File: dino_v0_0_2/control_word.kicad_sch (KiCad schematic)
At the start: 3 parts, among them U28 74LS138, U29 74LS138, U30 74LS138

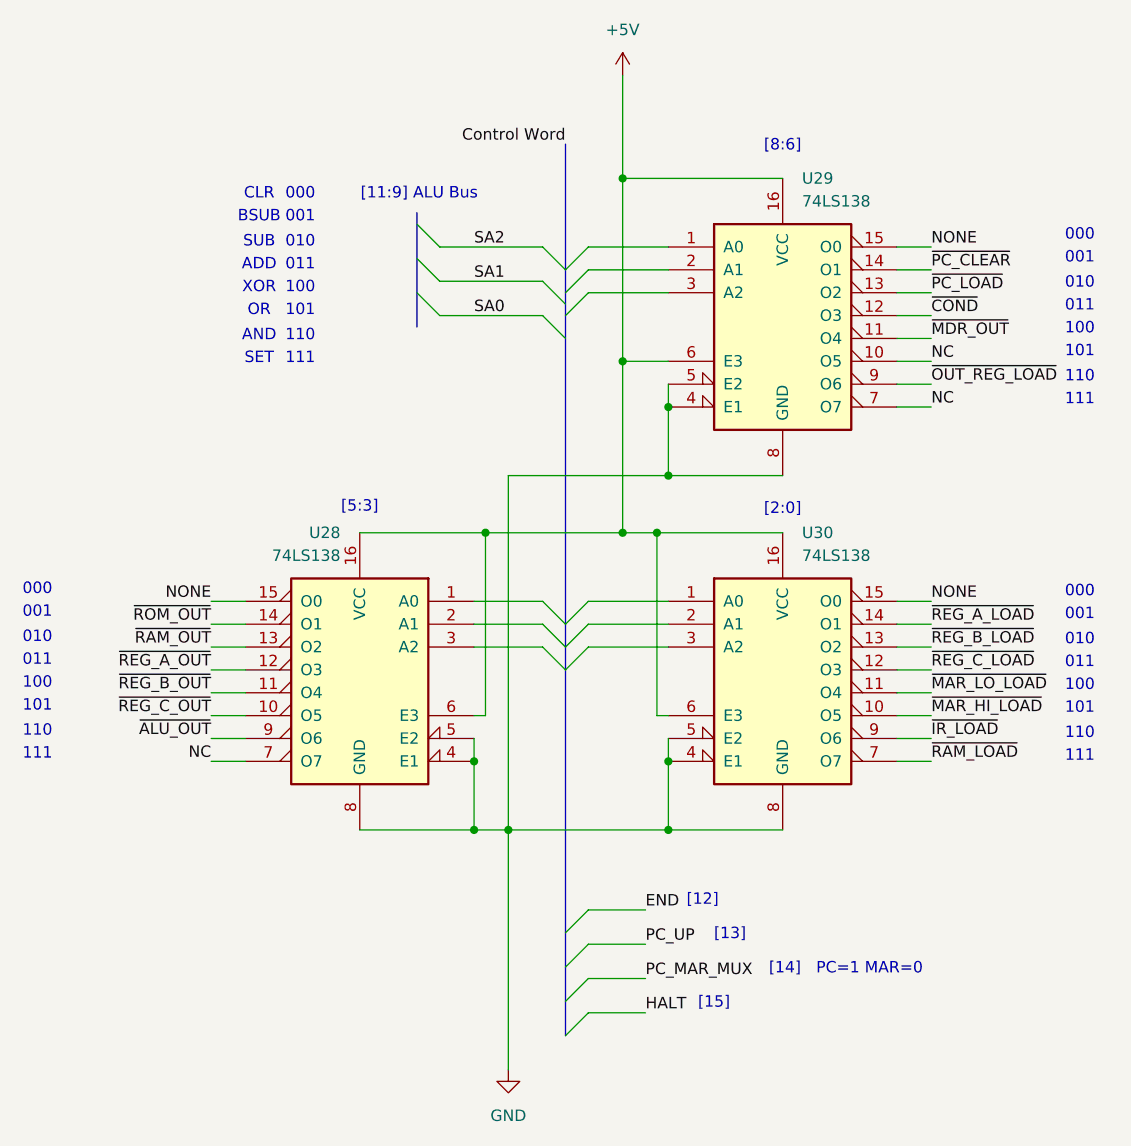
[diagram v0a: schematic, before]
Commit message: DINO v0.0.3: complete ALU/control-word, add MAR+reset sheets, wire reset circuit
ALU sheet: flags register moved from '173 (not in stock) to '273 + a '157
mux to emulate the missing load-enable pins; Z-detect built from a NOR+AND
De Morgan tree instead of a '260; ALU_CIN built from NAND(SA1,SA0) reusing
two already-placed spare gates instead of a dedicated XOR/'86. Sheet is
now fully wired and netlist-clean.

Control word sheet: all 16 CW bits assigned and wired (3x '138 decoders
for the load/source/misc fields, direct bus taps for HALT/PC_MAR_MUX/
PC_UP/END and the ALU SA[2:0] select). Found and fixed several cross-
sheet signal-name mismatches this uncovered (OUT_REG_LOAD/REG_OUT_LOAD,
PC_MAR_MUX/PC_MUX, T-state counter labels, a mirror-reversed IRB->ROM-
address buffer in microcode).

New: MAR and reset sheets, wired into the root hierarchy. Reset circuit
is a from-scratch design: RC+button+74HC14 Schmitt front end feeds the
async PRESET of the clock cluster's spare '74 half (U27B), synchronizing
release to CLK; its Q/~Q fan out to the flags register, the T-state
counter's clear, and (OR'd with the existing microcode-driven PC_CLEAR,
reusing spare gates on the same '02) the PC counters' clear.

Deprecated 7 schematic files no longer referenced by the root sheet's
hierarchy into dino_v0_0_2/deprecated/. Added docs/notes/kicad_netlist.py,
a .kicad_sch connectivity auditor (pin/net resolution incl. buses and
same-name local-label merging) used throughout this session to find the
above bugs; archived completed-work docs into docs/notes/Done/ and
rewrote dino_session_state.md as the current authoritative state+TODO.

Co-Authored-By: Claude Sonnet 5 <noreply@anthropic.com>
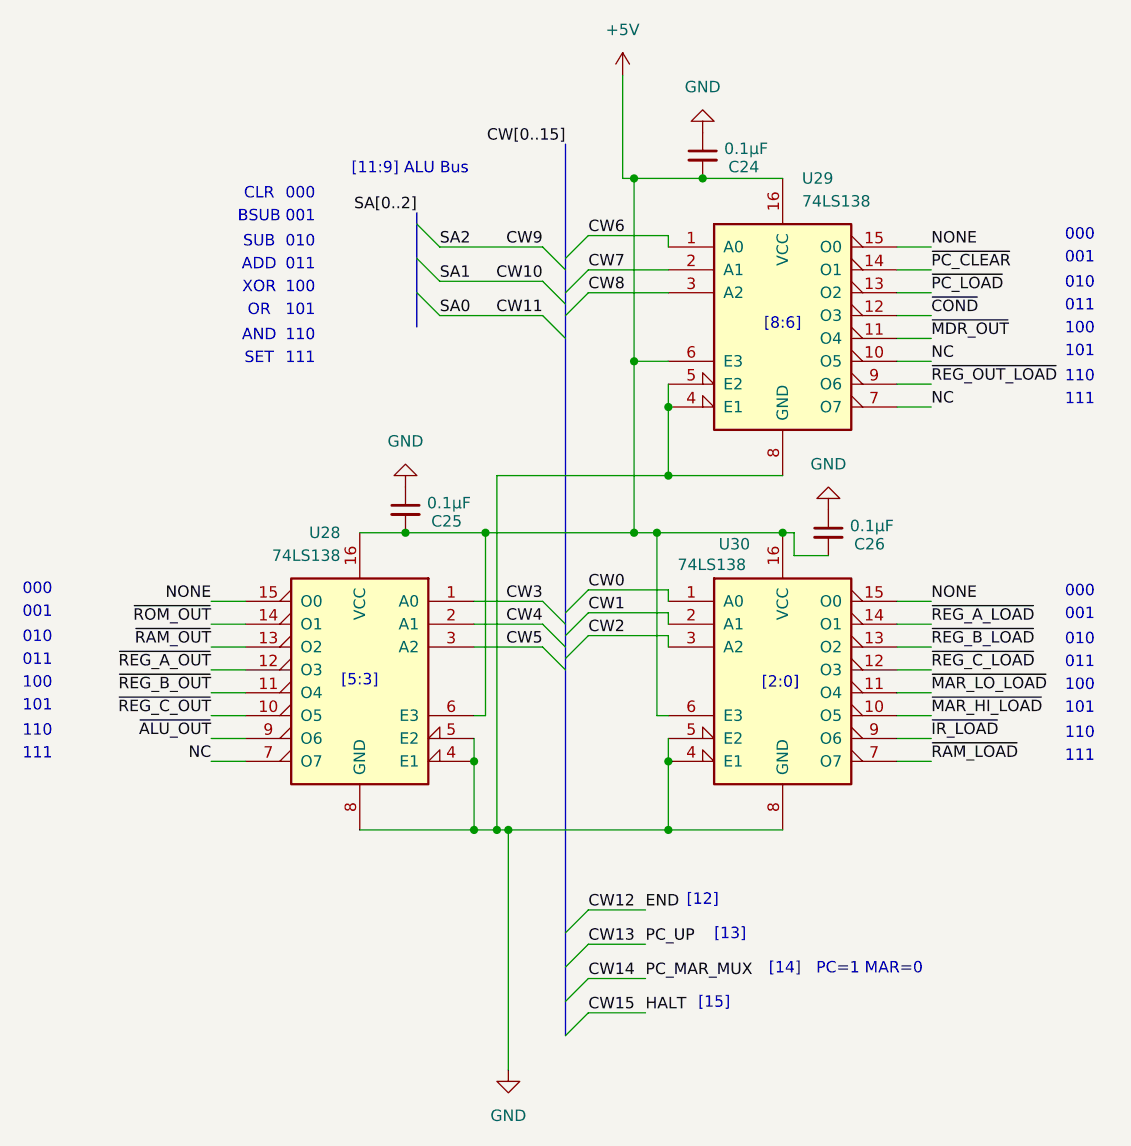
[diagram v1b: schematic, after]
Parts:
- added C24, C25, C26: 0.1µF, symbol Device:C_Small
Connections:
- net +5V: now also C24.2, C25.2, C26.2
- net GND: now also C24.1, C25.1, C26.1
- net CW3: now reaches U28.1 (A0)
- net CW4: now reaches U28.2 (A1)
- net CW5: now reaches U28.3 (A2)
- net CW0: now reaches U30.1 (A0)
- net CW1: now reaches U30.2 (A1)
- net CW2: now reaches U30.3 (A2)
- net CW6: now reaches U29.1 (A0)
- net CW7: now reaches U29.2 (A1)
- net CW8: now reaches U29.3 (A2)
- net ~{OUT_REG_LOAD} renamed ~{REG_OUT_LOAD}
